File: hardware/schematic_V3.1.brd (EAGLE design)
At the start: 77.7 x 62.1 mm, 22 parts, among them J1 POWER_JACKPTH, J2 ARDUINONANO, J3 ICSP, J4 ICSP, J5 2.54mm, J6 2.54mm, J7 2.54mm, J8 2.54mm, J9 2.54mm, U1 L9110S_DRIVER

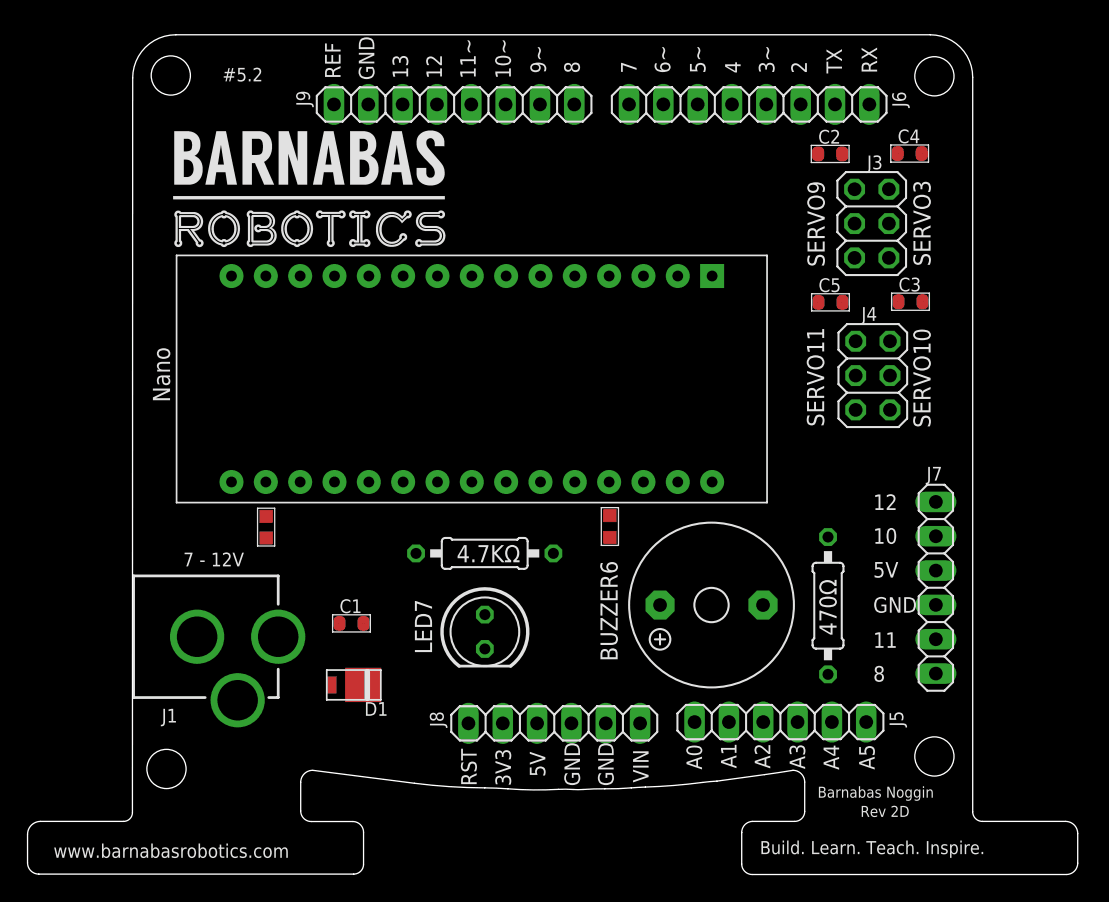
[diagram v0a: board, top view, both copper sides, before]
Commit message: Finished routing and change the logo
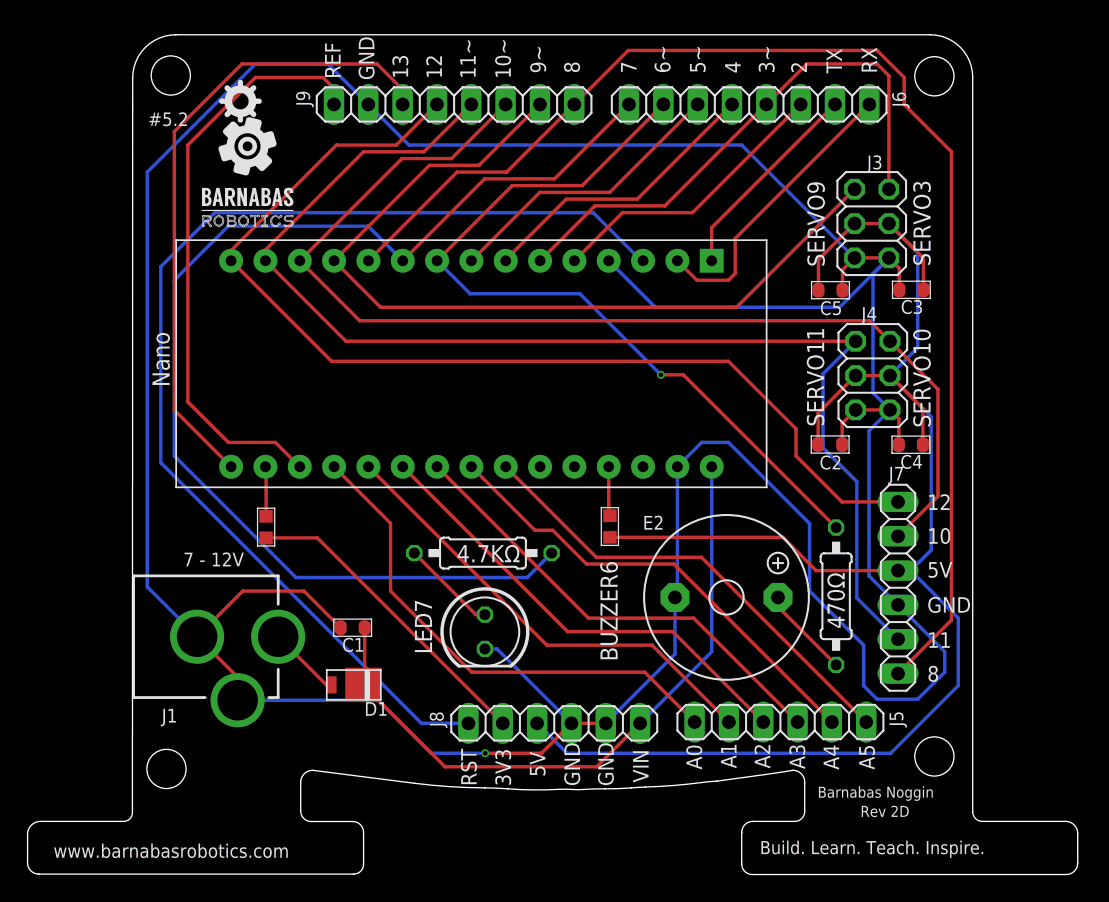
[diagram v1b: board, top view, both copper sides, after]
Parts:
- removed J2: ARDUINONANO, barnabas_noggin_V4:PDIP-32
- added U$1: ARDUINONANO, barnabas_noggin_V4:PDIP-32
- moved C4 21.5 mm to (65.5, 31.8), turned to 180 degrees
- moved C2 21.5 mm to (59.5, 31.8)
- moved J7 2.80 mm to (64.5, 21.2)
- moved E2 1.24 mm to (51.9, 20.5), turned to 0 degrees
- moved R2 0.92 mm to (60.0, 20.6)
- moved C5 0.90 mm to (59.5, 43.3)
- moved C3 0.88 mm to (65.5, 43.3), turned to 180 degrees
- moved C1 0.33 mm to (24.2, 18.3), turned to 180 degrees
- moved R1 0.13 mm to (33.8, 23.8), turned to 180 degrees
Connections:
- removed net 5V: C2.1, C3.1, C4.1, C5.1, F1.2, J2.+5V
- new net +5V: F1.2, U$1.+5V
- net 3V3: now also U$1.3V3; no longer J2.3V3
- net 5V_PIN: now also C2.1, C3.1, C4.1, C5.1
- net A0: now also U$1.A7; no longer J2.A7
- net A1: now also U$1.A6; no longer J2.A6
- net A2: now also U$1.A5; no longer J2.A5
- net A3: now also U$1.A4; no longer J2.A4
- net A4: now also U$1.A3; no longer J2.A3
- net A5: now also U$1.A2; no longer J2.A2
- net A6: now also U$1.A1; no longer J2.A1
- net A7: now also U$1.A0; no longer J2.A0
- net AREF: now also U$1.AREF; no longer J2.AREF
- net D10: now also U$1.D10; no longer J2.D10
- net D11/MOSI: now also U$1.D11; no longer J2.D11
- net D12/MISO: now also U$1.D12; no longer J2.D12
- net D13/SCK: now also U$1.D13; no longer J2.D13
- net D2: now also U$1.D2; no longer J2.D2
- net D3: now also U$1.D3; no longer J2.D3
- net D4: now also U$1.D4; no longer J2.D4
- net D5: now also U$1.D5; no longer J2.D5
- net D6: now also U$1.D6; no longer J2.D6
- net D7: now also U$1.D7; no longer J2.D7
- net D8: now also U$1.D8; no longer J2.D8
- net D9: now also U$1.D9; no longer J2.D9
- net GND: now also U$1.GND, U$1.GND1; no longer J2.GND, J2.GND1
- net RESET: now also U$1.RESET; no longer J2.RESET
- net RX: now also U$1.D0/RX; no longer J2.D0/RX
- net TX: now also U$1.D1/TX; no longer J2.D1/TX
- net VIN: now also U$1.VIN; no longer J2.VIN
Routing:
- net GND: track 0.00 -> 284.7 mm, vias 0 -> 1
- net 5V_PIN: track 0.00 -> 126.1 mm
- net D8: track 0.00 -> 94.1 mm
- net D11/MOSI: track 0.00 -> 92.0 mm
- net D7: track 0.00 -> 86.5 mm
- net RESET: track 0.00 -> 84.1 mm
- net D10: track 0.00 -> 83.3 mm
- net D12/MISO: track 0.00 -> 78.4 mm
- net D9: track 0.00 -> 63.6 mm
- net D6: track 0.00 -> 59.2 mm, vias 0 -> 1
- net VIN: track 0.00 -> 49.8 mm
- net D13/SCK: track 0.00 -> 47.4 mm
- net AREF: track 0.00 -> 43.7 mm
- net D3: track 0.00 -> 40.6 mm
- net A0: track 0.00 -> 37.4 mm
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
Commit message: Moved the logo and generated BOM
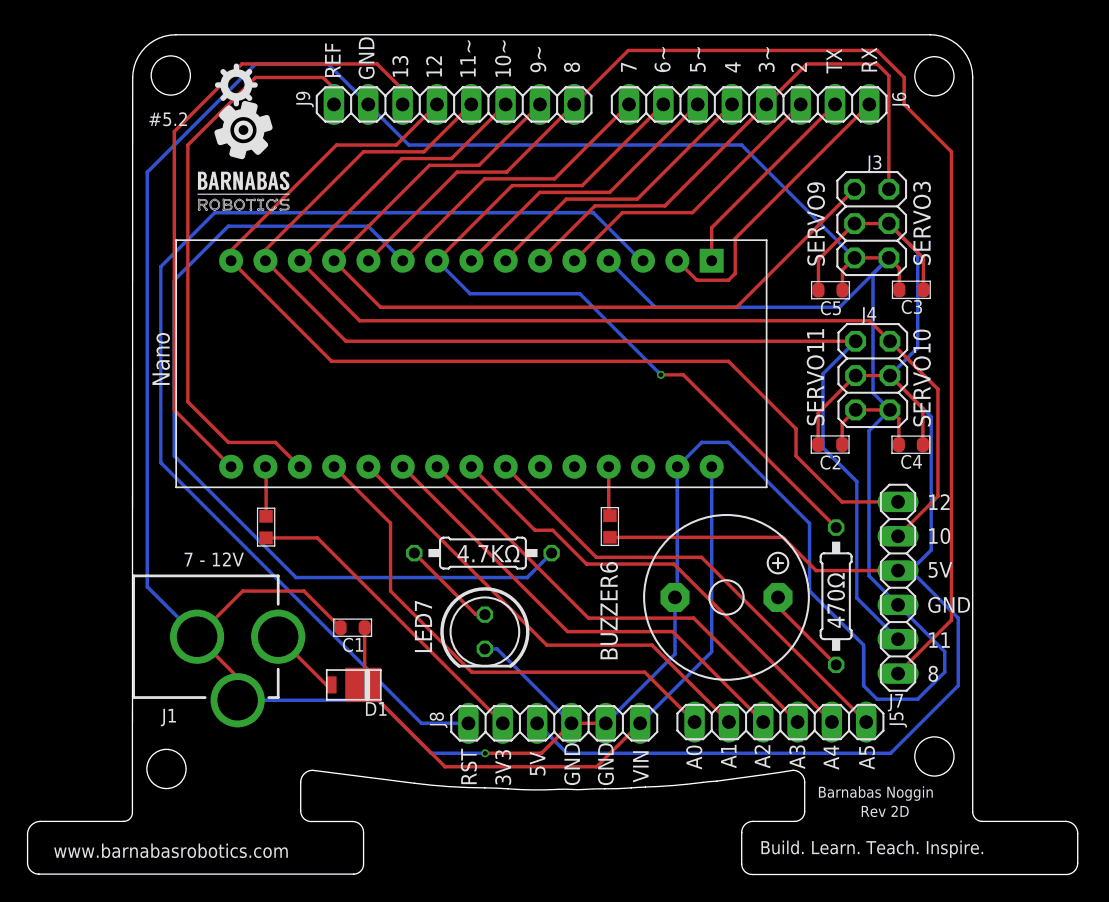
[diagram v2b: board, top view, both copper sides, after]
